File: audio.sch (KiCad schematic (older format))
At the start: 37 parts

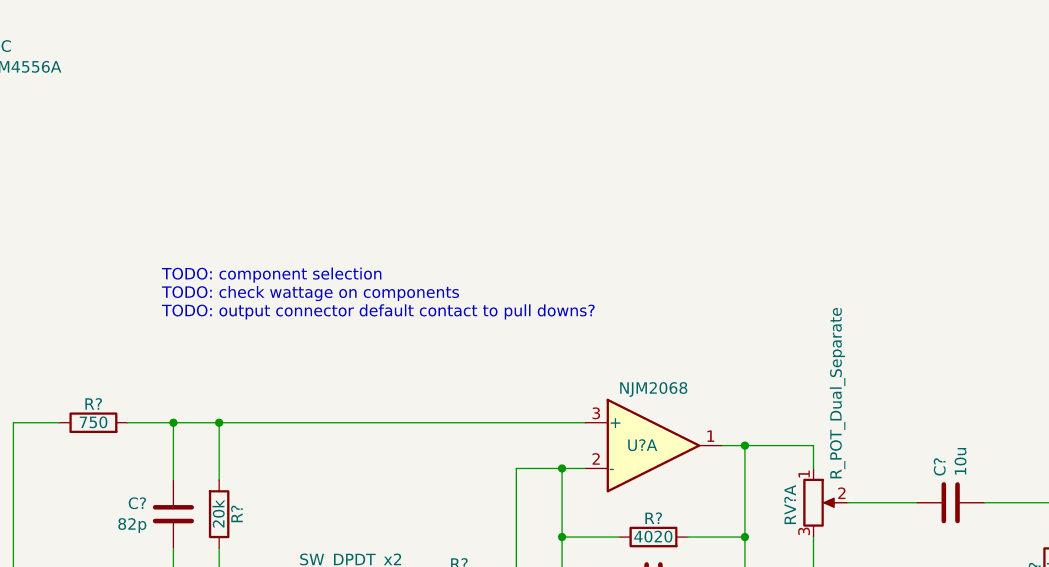
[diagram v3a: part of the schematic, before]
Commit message: add components for caps in audio.sch
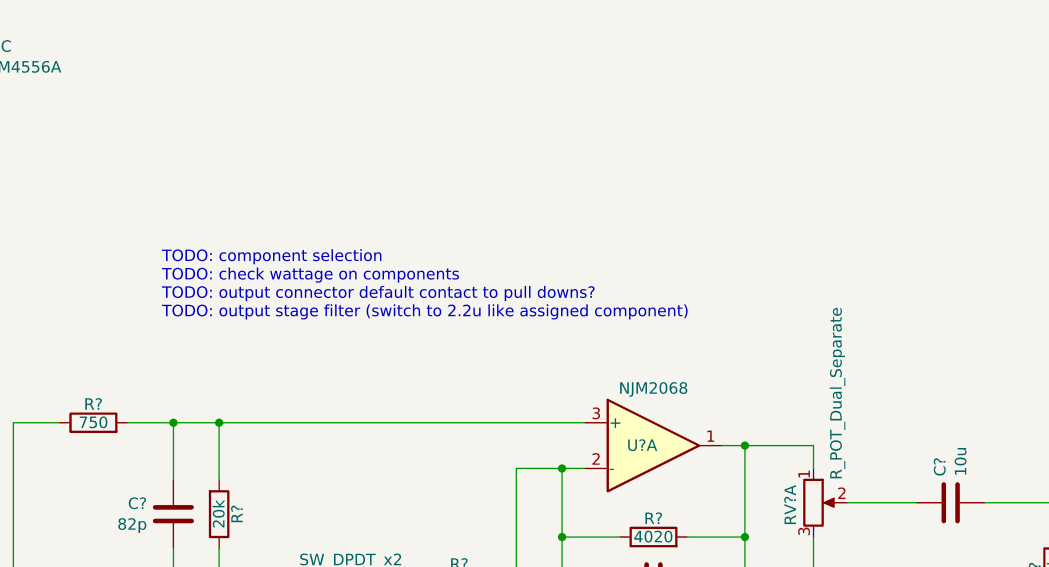
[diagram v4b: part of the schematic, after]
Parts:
- C? (x4): footprint (none) -> Capacitor_SMD:C_0805_2012Metric_Pad1.15x1.40mm_HandSolder; Description (none) -> CAP CER 82PF 50V NPO 0805; Manufacturer (none) -> Yageo; Manufacturer Part Number (none) -> CC0805FRNPO9BN820; Supplier (none) -> Digi-Key; Supplier Part Number (none) -> 311-4183-1-ND
- C? (x2): footprint (none) -> Capacitor_THT:C_Rect_L31.5mm_W11.0mm_P27.50mm_MKS4; Description (none) -> CAP FILM 2.2UF 5% 250VDC RAD; Manufacturer (none) -> WIMA; Manufacturer Part Number (none) -> MKP4F042206B00JSSD; Supplier (none) -> Digi-Key; Supplier Part Number (none) -> 1928-1546-ND
- J? (x2): Description (none) -> CONN JACK STEREO 1/4\" R/A; Manufacturer (none) -> Amphenol Sine Systems Corp; Manufacturer Part Number (none) -> ACJS-MHDR; Supplier (none) -> Digi-Key; Supplier Part Number (none) -> 889-1817-ND
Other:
- note added: "TODO: component selection\nTODO: check wattage on components\nTODO: output connector default contact to pull downs?\nTODO: output stage filter (switch to 2.2u like assigned component)"
- note removed: "TODO: component selection\nTODO: check wattage on components\nTODO: output connector default contact to pull downs?"
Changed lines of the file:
@@
 F 1 "AudioJack3_Switch" H 1968 4120 50  0000 R CNN
 F 2 "" H 2200 4100 50  0001 C CNN
-F 3 "~" H 2200 4100 50  0001 C CNN
+F 3 "https://www.amphenol-sine.com/pdf/datasheet/ACJS-MHDR.pdf" H 2200 4100 50  0001 C CNN
+F 4 "CONN JACK STEREO 1/4\" R/A" H 0   0   50  0001 C CNN "Description"
+F 5 "Amphenol Sine Systems Corp" H 0   0   50  0001 C CNN "Manufacturer"
+F 6 "ACJS-MHDR" H 0   0   50  0001 C CNN "Manufacturer Part Number"
+F 7 "Digi-Key" H 0   0   50  0001 C CNN "Supplier"
+F 8 "889-1817-ND" H 0   0   50  0001 C CNN "Supplier Part Number"
 	1    2200 4100
 	1    0    0    1
@@
 F 1 "AudioJack3_Switch" H 9318 4120 50  0000 R CNN
 F 2 "" H 9550 4100 50  0001 C CNN
-F 3 "~" H 9550 4100 50  0001 C CNN
+F 3 "https://www.amphenol-sine.com/pdf/datasheet/ACJS-MHDR.pdf" H 9550 4100 50  0001 C CNN
+F 4 "CONN JACK STEREO 1/4\" R/A" H 0   0   50  0001 C CNN "Description"
+F 5 "Amphenol Sine Systems Corp" H 0   0   50  0001 C CNN "Manufacturer"
+F 6 "ACJS-MHDR" H 0   0   50  0001 C CNN "Manufacturer Part Number"
+F 7 "Digi-Key" H 0   0   50  0001 C CNN "Supplier"
+F 8 "889-1817-ND" H 0   0   50  0001 C CNN "Supplier Part Number"
 	1    9550 4100
 	-1   0    0    1
@@
 F 0 "C?" H 5485 3554 50  0000 R CNN
 F 1 "82p" H 5485 3645 50  0000 R CNN
-F 2 "" H 5638 3450 50  0001 C CNN
-F 3 "" H 5600 3600 50  0001 C CNN
-F 4 "" H 3150 -1550 50  0001 C CNN "Description"
-F 5 "" H 3150 -1550 50  0001 C CNN "Manufacturer"
-F 6 "" H 3150 -1550 50  0001 C CNN "Manufacturer Part Number"
-F 7 "" H 3150 -1550 50  0001 C CNN "Supplier"
-F 8 "" H 3150 -1550 50  0001 C CNN "Supplier Part Number"
+F 2 "Capacitor_SMD:C_0805_2012Metric_Pad1.15x1.40mm_HandSolder" H 5638 3450 50  0001 C CNN
+F 3 "http://www.yageo.com/documents/recent/UPY-GP_NP0_16V-to-50V_16.pdf" H 5600 3600 50  0001 C CNN
+F 4 "CAP CER 82PF 50V NPO 0805" H 3150 -1550 50  0001 C CNN "Description"
+F 5 "Yageo" H 3150 -1550 50  0001 C CNN "Manufacturer"
+F 6 "CC0805FRNPO9BN820" H 3150 -1550 50  0001 C CNN "Manufacturer Part Number"
+F 7 "Digi-Key" H 3150 -1550 50  0001 C CNN "Supplier"
+F 8 "311-4183-1-ND" H 3150 -1550 50  0001 C CNN "Supplier Part Number"
 	1    5600 3600
 	0    1    -1   0
@@
 F 0 "C?" H 5485 4354 50  0000 R CNN
 F 1 "82p" H 5485 4445 50  0000 R CNN
-F 2 "" H 5638 4250 50  0001 C CNN
-F 3 "" H 5600 4400 50  0001 C CNN
-F 4 "" H 3150 -750 50  0001 C CNN "Description"
-F 5 "" H 3150 -750 50  0001 C CNN "Manufacturer"
-F 6 "" H 3150 -750 50  0001 C CNN "Manufacturer Part Number"
-F 7 "" H 3150 -750 50  0001 C CNN "Supplier"
-F 8 "" H 3150 -750 50  0001 C CNN "Supplier Part Number"
+F 2 "Capacitor_SMD:C_0805_2012Metric_Pad1.15x1.40mm_HandSolder" H 5638 4250 50  0001 C CNN
+F 3 "http://www.yageo.com/documents/recent/UPY-GP_NP0_16V-to-50V_16.pdf" H 5600 4400 50  0001 C CNN
+F 4 "CAP CER 82PF 50V NPO 0805" H 3150 -750 50  0001 C CNN "Description"
+F 5 "Yageo" H 3150 -750 50  0001 C CNN "Manufacturer"
+F 6 "CC0805FRNPO9BN820" H 3150 -750 50  0001 C CNN "Manufacturer Part Number"
+F 7 "Digi-Key" H 3150 -750 50  0001 C CNN "Supplier"
+F 8 "311-4183-1-ND" H 3150 -750 50  0001 C CNN "Supplier Part Number"
 	1    5600 4400
 	0    1    1    0
@@
 F 0 "C?" H 3385 3254 50  0000 R CNN
 F 1 "82p" H 3385 3345 50  0000 R CNN
-F 2 "" H 3538 3150 50  0001 C CNN
-F 3 "" H 3500 3300 50  0001 C CNN
-F 4 "" H 1050 -1850 50  0001 C CNN "Description"
-F 5 "" H 1050 -1850 50  0001 C CNN "Manufacturer"
-F 6 "" H 1050 -1850 50  0001 C CNN "Manufacturer Part Number"
-F 7 "" H 1050 -1850 50  0001 C CNN "Supplier"
-F 8 "" H 1050 -1850 50  0001 C CNN "Supplier Part Number"
+F 2 "Capacitor_SMD:C_0805_2012Metric_Pad1.15x1.40mm_HandSolder" H 3538 3150 50  0001 C CNN
+F 3 "http://www.yageo.com/documents/recent/UPY-GP_NP0_16V-to-50V_16.pdf" H 3500 3300 50  0001 C CNN
+F 4 "CAP CER 82PF 50V NPO 0805" H 1050 -1850 50  0001 C CNN "Description"
+F 5 "Yageo" H 1050 -1850 50  0001 C CNN "Manufacturer"
+F 6 "CC0805FRNPO9BN820" H 1050 -1850 50  0001 C CNN "Manufacturer Part Number"
+F 7 "Digi-Key" H 1050 -1850 50  0001 C CNN "Supplier"
+F 8 "311-4183-1-ND" H 1050 -1850 50  0001 C CNN "Supplier Part Number"
 	1    3500 3300
 	1    0    0    1
@@
 F 0 "C?" H 3385 4654 50  0000 R CNN
 F 1 "82p" H 3385 4745 50  0000 R CNN
-F 2 "" H 3538 4550 50  0001 C CNN
-F 3 "" H 3500 4700 50  0001 C CNN
-F 4 "" H 1050 -450 50  0001 C CNN "Description"
-F 5 "" H 1050 -450 50  0001 C CNN "Manufacturer"
-F 6 "" H 1050 -450 50  0001 C CNN "Manufacturer Part Number"
-F 7 "" H 1050 -450 50  0001 C CNN "Supplier"
-F 8 "" H 1050 -450 50  0001 C CNN "Supplier Part Number"
+F 2 "Capacitor_SMD:C_0805_2012Metric_Pad1.15x1.40mm_HandSolder" H 3538 4550 50  0001 C CNN
+F 3 "http://www.yageo.com/documents/recent/UPY-GP_NP0_16V-to-50V_16.pdf" H 3500 4700 50  0001 C CNN
+F 4 "CAP CER 82PF 50V NPO 0805" H 1050 -450 50  0001 C CNN "Description"
+F 5 "Yageo" H 1050 -450 50  0001 C CNN "Manufacturer"
+F 6 "CC0805FRNPO9BN820" H 1050 -450 50  0001 C CNN "Manufacturer Part Number"
+F 7 "Digi-Key" H 1050 -450 50  0001 C CNN "Supplier"
+F 8 "311-4183-1-ND" H 1050 -450 50  0001 C CNN "Supplier Part Number"
 	1    3500 4700
 	1    0    0    -1
@@
 	3700 4000 3700 4300
 Text Notes 3450 2450 0    50   ~ 0
-TODO: component selection\nTODO: check wattage on components\nTODO: output connector default contact to pull downs?
+TODO: component selection\nTODO: check wattage on components\nTODO: output connector default contact to pull downs?\nTODO: output stage filter (switch to 2.2u like assigned component)
 $Comp
 L Amplifier_Operational:NJM4556A U?
@@
 F 0 "C?" H 6785 3204 50  0000 R CNN
 F 1 "10u" H 6785 3295 50  0000 R CNN
-F 2 "" H 6938 3100 50  0001 C CNN
-F 3 "" H 6900 3250 50  0001 C CNN
-F 4 "" H 4450 -1900 50  0001 C CNN "Description"
-F 5 "" H 4450 -1900 50  0001 C CNN "Manufacturer"
-F 6 "" H 4450 -1900 50  0001 C CNN "Manufacturer Part Number"
-F 7 "" H 4450 -1900 50  0001 C CNN "Supplier"
-F 8 "" H 4450 -1900 50  0001 C CNN "Supplier Part Number"
+F 2 "Capacitor_THT:C_Rect_L31.5mm_W11.0mm_P27.50mm_MKS4" H 6938 3100 50  0001 C CNN
+F 3 "https://www.wima.de/wp-content/uploads/media/e_WIMA_MKP_4.pdf" H 6900 3250 50  0001 C CNN
+F 4 "CAP FILM 2.2UF 5% 250VDC RAD" H 4450 -1900 50  0001 C CNN "Description"
+F 5 "WIMA" H 4450 -1900 50  0001 C CNN "Manufacturer"
+F 6 "MKP4F042206B00JSSD" H 4450 -1900 50  0001 C CNN "Manufacturer Part Number"
+F 7 "Digi-Key" H 4450 -1900 50  0001 C CNN "Supplier"
+F 8 "1928-1546-ND" H 4450 -1900 50  0001 C CNN "Supplier Part Number"
 	1    6900 3250
 	0    1    1    0
@@
 F 0 "C?" H 6785 4704 50  0000 R CNN
 F 1 "10u" H 6785 4795 50  0000 R CNN
-F 2 "" H 6938 4600 50  0001 C CNN
-F 3 "" H 6900 4750 50  0001 C CNN
-F 4 "" H 4450 -400 50  0001 C CNN "Description"
-F 5 "" H 4450 -400 50  0001 C CNN "Manufacturer"
-F 6 "" H 4450 -400 50  0001 C CNN "Manufacturer Part Number"
-F 7 "" H 4450 -400 50  0001 C CNN "Supplier"
-F 8 "" H 4450 -400 50  0001 C CNN "Supplier Part Number"
+F 2 "Capacitor_THT:C_Rect_L31.5mm_W11.0mm_P27.50mm_MKS4" H 6938 4600 50  0001 C CNN
+F 3 "https://www.wima.de/wp-content/uploads/media/e_WIMA_MKP_4.pdf" H 6900 4750 50  0001 C CNN
+F 4 "CAP FILM 2.2UF 5% 250VDC RAD" H 4450 -400 50  0001 C CNN "Description"
+F 5 "WIMA" H 4450 -400 50  0001 C CNN "Manufacturer"
+F 6 "MKP4F042206B00JSSD" H 4450 -400 50  0001 C CNN "Manufacturer Part Number"
+F 7 "Digi-Key" H 4450 -400 50  0001 C CNN "Supplier"
+F 8 "1928-1546-ND" H 4450 -400 50  0001 C CNN "Supplier Part Number"
 	1    6900 4750
 	0    1    -1   0

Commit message: add components for audo.sch
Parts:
- R? (x2): Description RES SMD 1.82M OHM 1% 1/8W 0805 -> RES SMD 3.24K OHM 0.1% 1/8W 0805 Metal Film; Manufacturer Part Number ERJ-6ENF1824V -> ERA-6AEB3241V; Supplier Part Number P1.82BTCT-ND -> P3.24KDACT-ND
- R? (x4): Description RES SMD 1.82M OHM 1% 1/8W 0805 -> RES SMD 750 OHM 0.1% 1/8W 0805 Metal Film; Manufacturer Part Number ERJ-6ENF1824V -> ERA-6AEB751V; Supplier Part Number P1.82BTCT-ND -> P750DACT-ND
- R? (x2): Description RES SMD 1.82M OHM 1% 1/8W 0805 -> RES SMD 4.02K OHM 0.1% 1/8W 0805 Metal Film; Manufacturer Part Number ERJ-6ENF1824V -> ERA-6AEB4021V; Supplier Part Number P1.82BTCT-ND -> P4.02KDACT-ND
- R? (x4): Description RES SMD 1.82M OHM 1% 1/8W 0805 -> RES SMD 20K OHM 0.1% 1/8W 0805 Metal Film; Manufacturer Part Number ERJ-6ENF1824V -> ERA-6AEB203V; Supplier Part Number P1.82BTCT-ND -> P20KDACT-ND
- R? (x4): footprint Resistor_SMD:R_0805_2012Metric_Pad1.15x1.40mm_HandSolder -> (none); Description RES SMD 1.82M OHM 1% 1/8W 0805 -> (none); Manufacturer Panasonic Electronic Components -> (none); Manufacturer Part Number ERJ-6ENF1824V -> (none); Supplier Digi-Key -> (none); Supplier Part Number P1.82BTCT-ND -> (none)

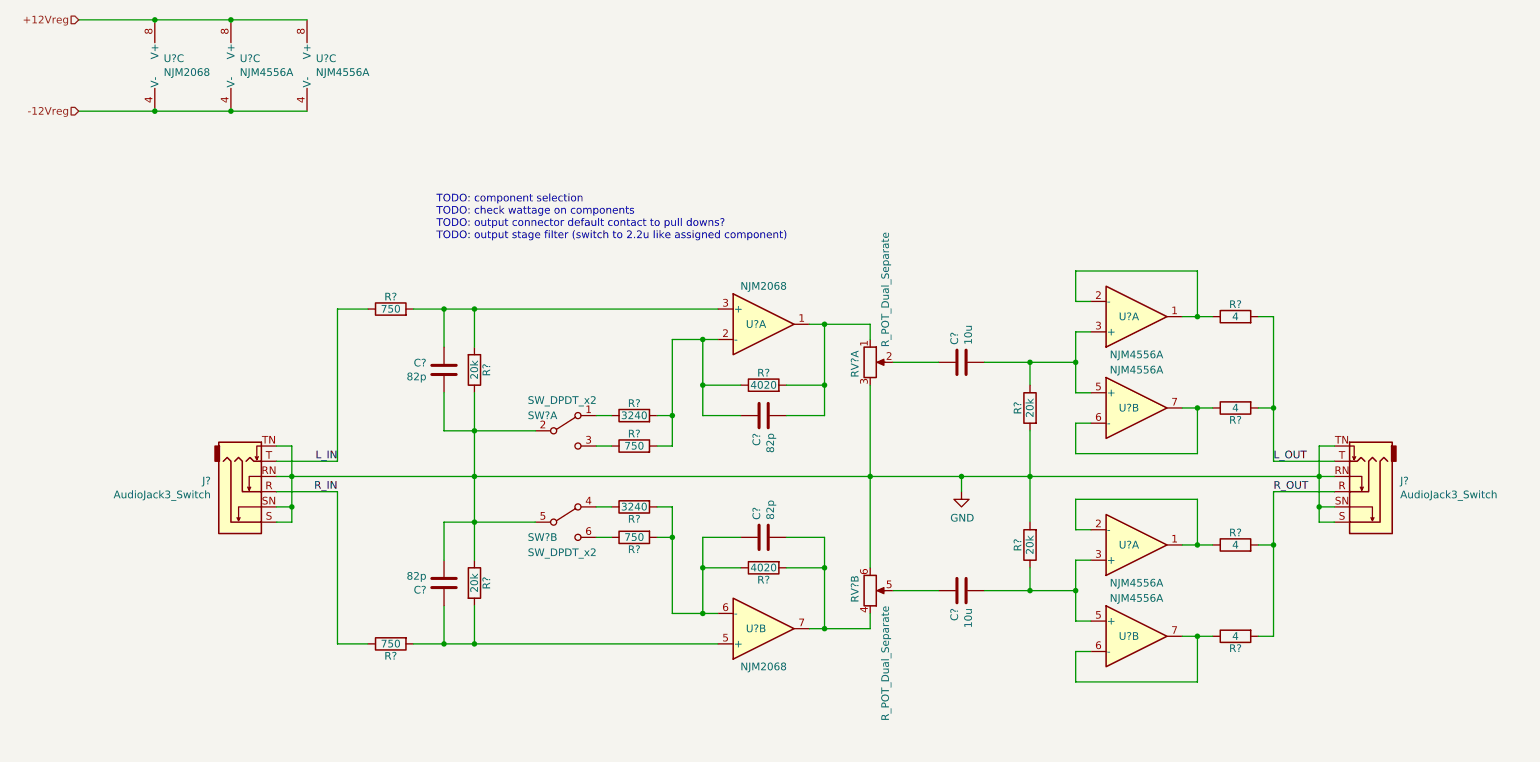
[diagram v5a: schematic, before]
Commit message: update audio jack connections
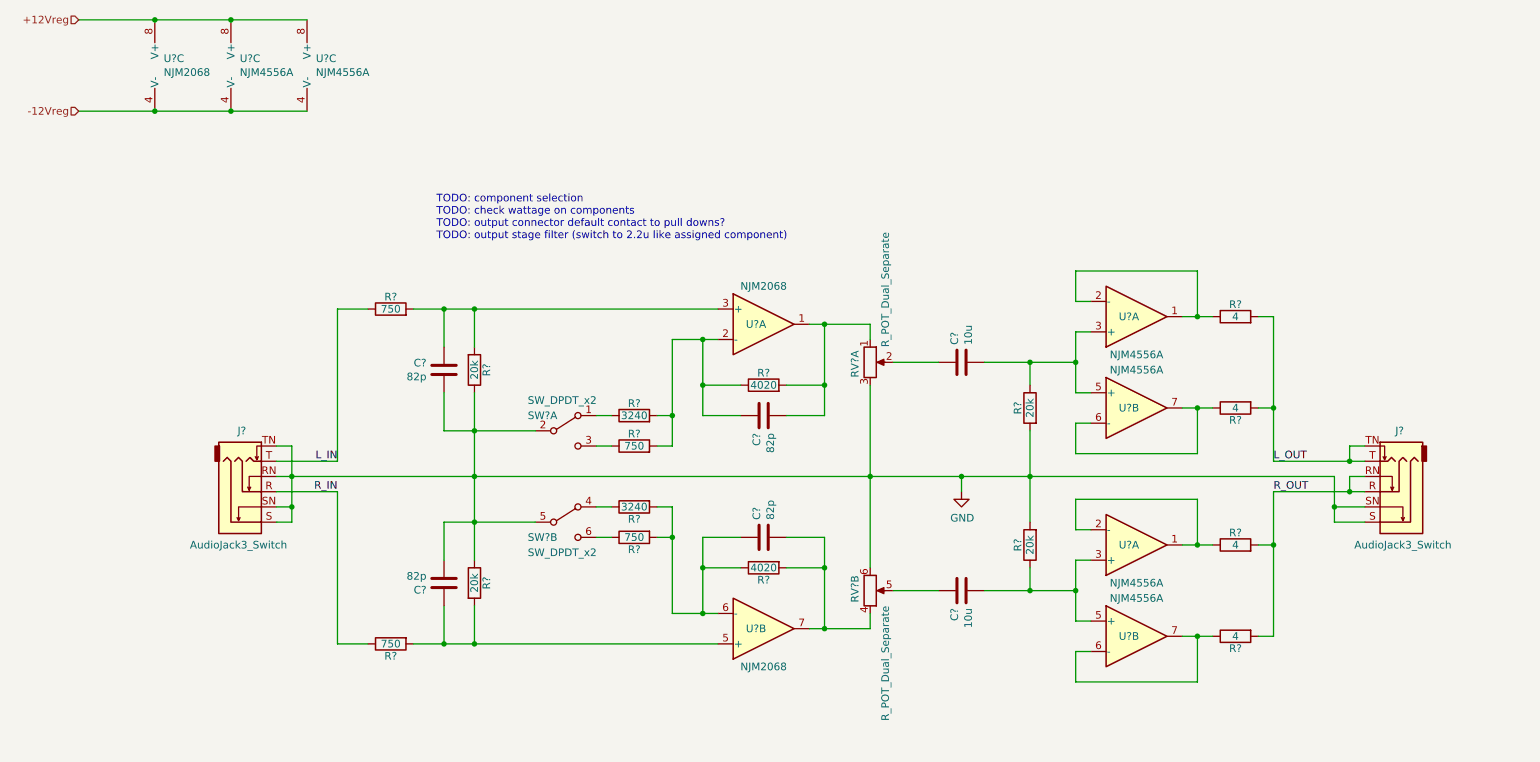
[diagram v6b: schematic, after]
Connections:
- net GND: no longer J?.RN, J?.TN
- net L_OUT: now also J?.TN
- net R_OUT: now also J?.RN
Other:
- moved on the sheet: J?
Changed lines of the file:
@@
 U 1 1 5CB56C98
 P 2200 4100
-F 0 "J?" H 1968 4029 50  0000 R CNN
-F 1 "AudioJack3_Switch" H 1968 4120 50  0000 R CNN
+F 0 "J?" H 2200 3700 50  0000 R CNN
+F 1 "AudioJack3_Switch" H 2150 4450 50  0000 C CNN
 F 2 "" H 2200 4100 50  0001 C CNN
 F 3 "https://www.amphenol-sine.com/pdf/datasheet/ACJS-MHDR.pdf" H 2200 4100 50  0001 C CNN
@@
 L Connector:AudioJack3_Switch J?
 U 1 1 5CB57002
-P 9550 4100
-F 0 "J?" H 9318 4029 50  0000 R CNN
-F 1 "AudioJack3_Switch" H 9318 4120 50  0000 R CNN
-F 2 "" H 9550 4100 50  0001 C CNN
-F 3 "https://www.amphenol-sine.com/pdf/datasheet/ACJS-MHDR.pdf" H 9550 4100 50  0001 C CNN
-F 4 "CONN JACK STEREO 1/4\" R/A" H 0   0   50  0001 C CNN "Description"
-F 5 "Amphenol Sine Systems Corp" H 0   0   50  0001 C CNN "Manufacturer"
-F 6 "ACJS-MHDR" H 0   0   50  0001 C CNN "Manufacturer Part Number"
-F 7 "Digi-Key" H 0   0   50  0001 C CNN "Supplier"
-F 8 "889-1817-ND" H 0   0   50  0001 C CNN "Supplier Part Number"
-	1    9550 4100
+P 9750 4100
+F 0 "J?" H 9750 3700 50  0000 R CNN
+F 1 "AudioJack3_Switch" H 9700 4450 50  0000 C CNN
+F 2 "" H 9750 4100 50  0001 C CNN
+F 3 "https://www.amphenol-sine.com/pdf/datasheet/ACJS-MHDR.pdf" H 9750 4100 50  0001 C CNN
+F 4 "CONN JACK STEREO 1/4\" R/A" H 200 0   50  0001 C CNN "Description"
+F 5 "Amphenol Sine Systems Corp" H 200 0   50  0001 C CNN "Manufacturer"
+F 6 "ACJS-MHDR" H 200 0   50  0001 C CNN "Manufacturer Part Number"
+F 7 "Digi-Key" H 200 0   50  0001 C CNN "Supplier"
+F 8 "889-1817-ND" H 200 0   50  0001 C CNN "Supplier Part Number"
+	1    9750 4100
 	-1   0    0    1
 $EndComp
 Wire Wire Line
-	9350 4300 9250 4300
-Wire Wire Line
-	9350 4200 9250 4200
-Wire Wire Line
-	9250 4200 9250 4300
-Wire Wire Line
-	8950 4100 9350 4100
-Wire Wire Line
-	8950 3900 9350 3900
+	9550 4300 9350 4300
+Wire Wire Line
+	9550 4200 9350 4200
+Wire Wire Line
+	9350 4200 9350 4300
+Wire Wire Line
+	8950 4100 9450 4100
 Text Label 8950 3900 0    50   ~ 0
 L_OUT
@@
 Connection ~ 8950 3550
 Wire Wire Line
-	9350 4000 9250 4000
-Wire Wire Line
-	9250 4000 9250 4200
-Connection ~ 9250 4200
-Wire Wire Line
-	9350 3800 9250 3800
-Wire Wire Line
-	9250 3800 9250 4000
-Connection ~ 9250 4000
-Wire Wire Line
-	9250 4000 7350 4000
+	9550 3800 9450 3800
 $Comp
 L Device:R_POT_Dual_Separate RV?
@@
 Connection ~ 2100 1000
 Connection ~ 1600 1000
+Wire Wire Line
+	9450 4100 9450 4000
+Wire Wire Line
+	9450 4000 9550 4000
+Connection ~ 9450 4100
+Wire Wire Line
+	9450 4100 9550 4100
+Wire Wire Line
+	8950 3900 9450 3900
+Wire Wire Line
+	9450 3800 9450 3900
+Connection ~ 9450 3900
+Wire Wire Line
+	9450 3900 9550 3900
+Wire Wire Line
+	7350 4000 9350 4000
+Wire Wire Line
+	9350 4000 9350 4200
+Connection ~ 9350 4200
 $EndSCHEMATC
